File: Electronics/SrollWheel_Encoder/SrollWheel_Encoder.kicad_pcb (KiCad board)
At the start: 2 copper layers, 6 parts

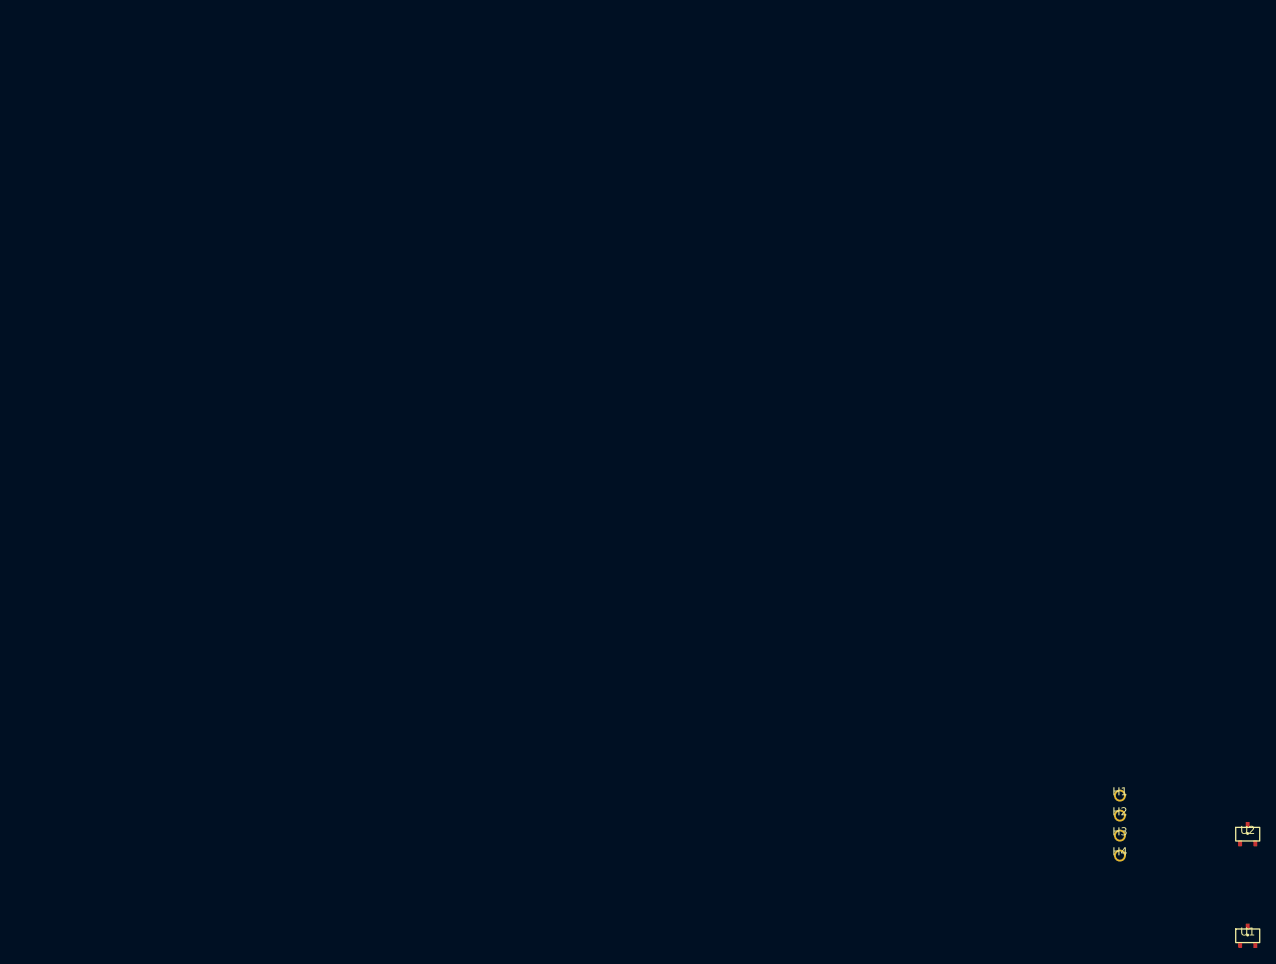
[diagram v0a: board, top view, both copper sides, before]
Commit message: started the scroll wheel pcb
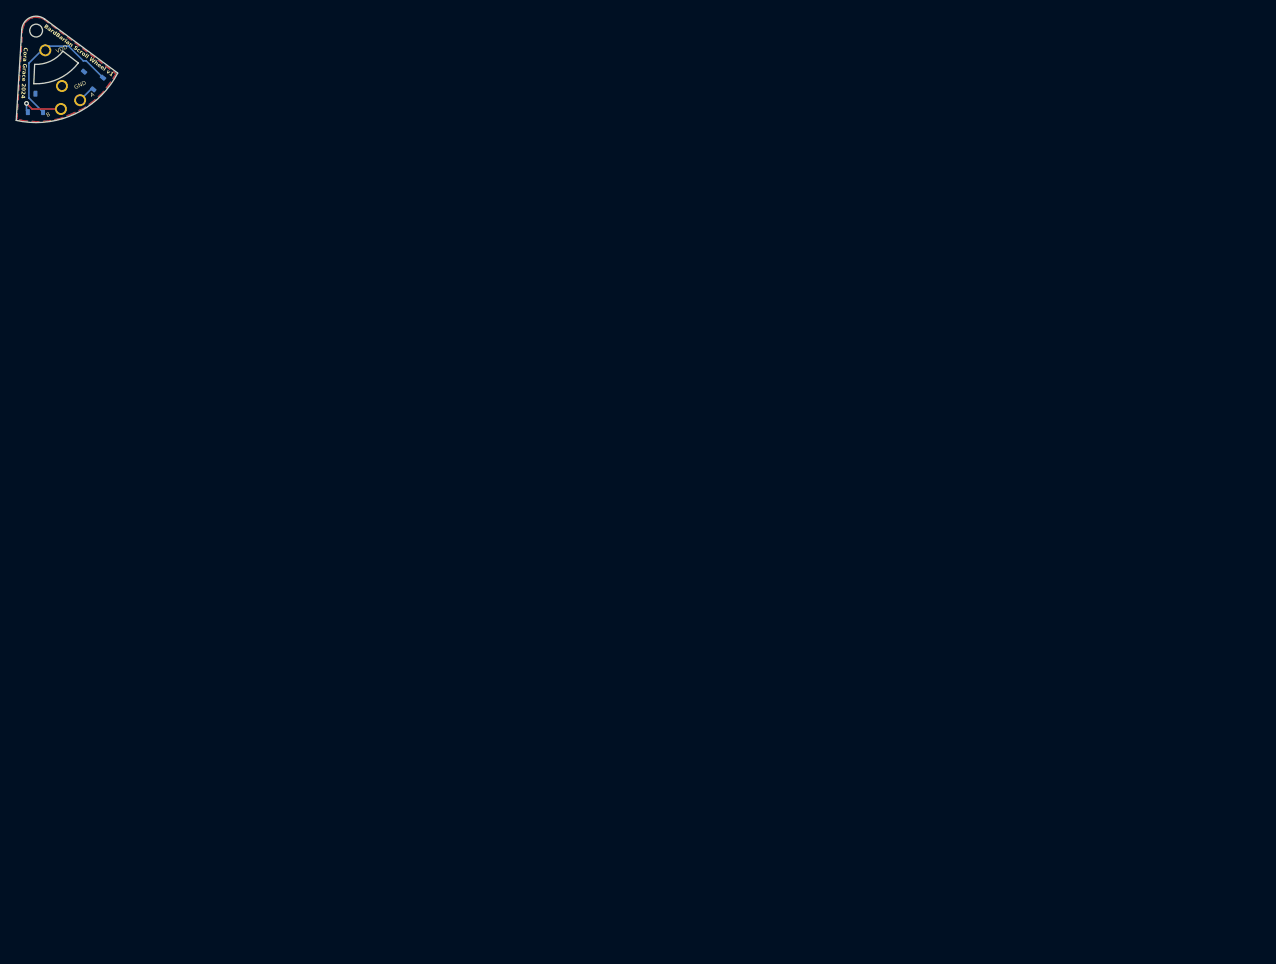
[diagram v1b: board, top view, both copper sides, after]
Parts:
- U1, U2: moved to B.Cu
- moved U1 180.0 mm to (6.87, 5.88), turned to -130 degrees
- moved U2 177.0 mm to (-0.08, 9.04), turned to 180 degrees
- moved VDD 163.5 mm to (1.15, 2.47), turned to 25 degrees
- moved B 162.0 mm to (3.10, 9.80), turned to 25 degrees
- moved GND 160.6 mm to (3.23, 6.93), turned to 25 degrees
- moved A 159.2 mm to (5.50, 8.70), turned to 25 degrees
- renumbered H3 to A, H4 to B, H2 to GND, H1 to VDD
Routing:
- net /VDD: track 0.00 -> 18.6 mm
- net /B: track 0.00 -> 5.75 mm, vias 0 -> 1
- net /A: track 0.00 -> 2.21 mm
- added copper zone on B.Cu, net /GND
- added copper zone on F.Cu, net /GND
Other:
- board outline added: 12.7 x 13.3 mm
- board text added: "BardBarian Scroll Wheel v1"
- board text added: "Cora Grace 2024"
